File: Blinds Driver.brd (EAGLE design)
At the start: 100 x 80 mm, 29 parts

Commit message: Shrinkage!
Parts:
- moved TIME_DIP 34.2 mm to (14.0, 26.7), turned to 90 degrees
- moved GO_DOWN 20.9 mm to (34.3, 66.0)
- moved GO_UP 18.5 mm to (25.4, 66.0)
- moved R8 12.5 mm to (57.1, 53.3), turned to 270 degrees
- moved ADDLARGETIME 11.7 mm to (52.1, 66.0)
- moved ADDSMALLTIME 11.4 mm to (43.2, 66.0)
- moved D1 6.35 mm to (69.8, 16.5)
- moved D2 6.35 mm to (69.8, 50.8)
- moved D5 6.35 mm to (73.7, 50.8)
- moved D7 6.35 mm to (73.7, 43.2)
- moved D8 6.35 mm to (73.7, 25.4)
- moved MOTOR_OUT 6.35 mm to (87.6, 71.1)
- moved R7 6.35 mm to (59.7, 19.1)
- moved H_BRIDGE 6.35 mm to (61.0, 33.0)
- moved D3 6.35 mm to (76.2, 29.2)
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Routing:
- net N$19: track 30.2 -> 58.2 mm
- net N$18: track 21.2 -> 48.3 mm
- net N$21: track 55.4 -> 32.4 mm
- net N$4: track 19.1 -> 41.3 mm
- net N$5: track 15.5 -> 35.2 mm
- net N$7: track 12.0 -> 27.3 mm
- net +5V: track 112.6 -> 102.4 mm
- net N$20: track 49.8 -> 39.8 mm
- net N$3: track 38.4 -> 30.6 mm
- net N$1: track 29.0 -> 21.2 mm
- net N$22: track 40.9 -> 34.4 mm
- net N$2: track 22.9 -> 16.5 mm
- net N$24: track 46.8 -> 44.5 mm
- net N$9: track 16.3 -> 17.9 mm

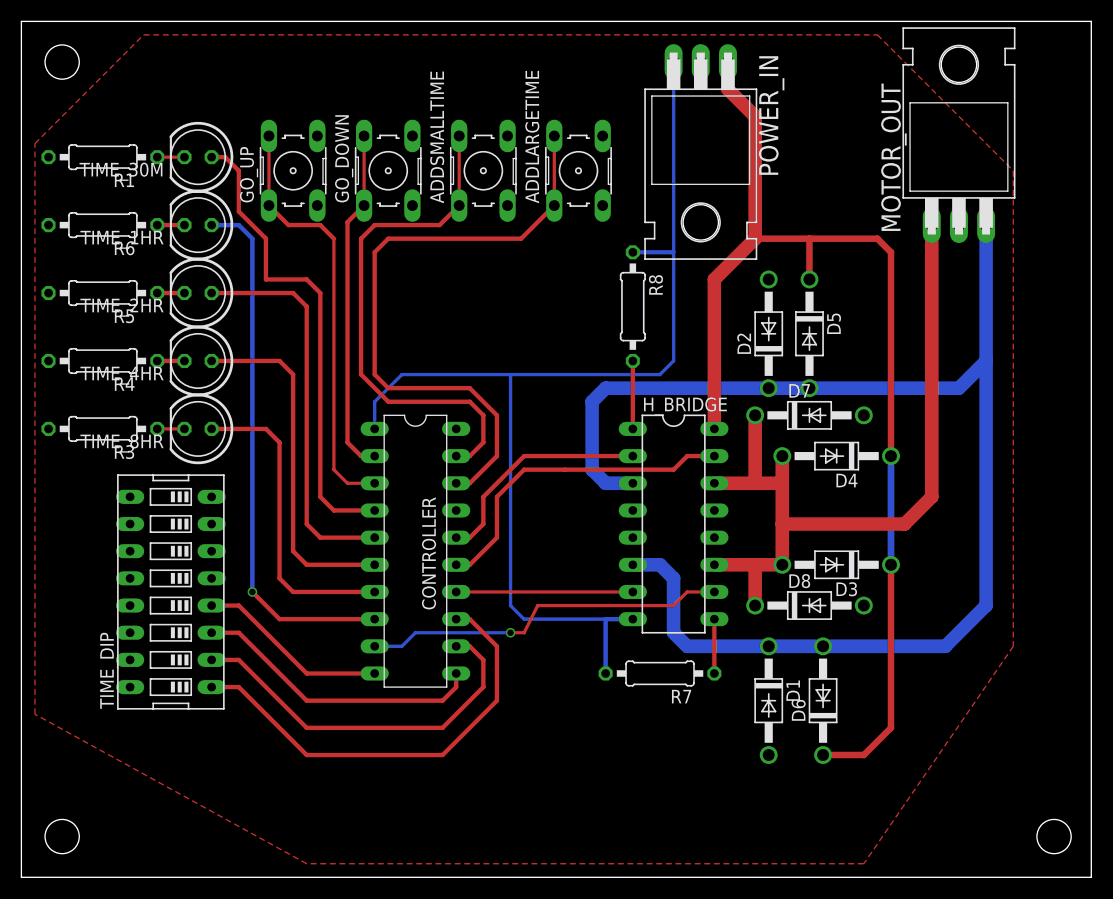
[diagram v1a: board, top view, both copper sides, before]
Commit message: Miniaturize and remove last via
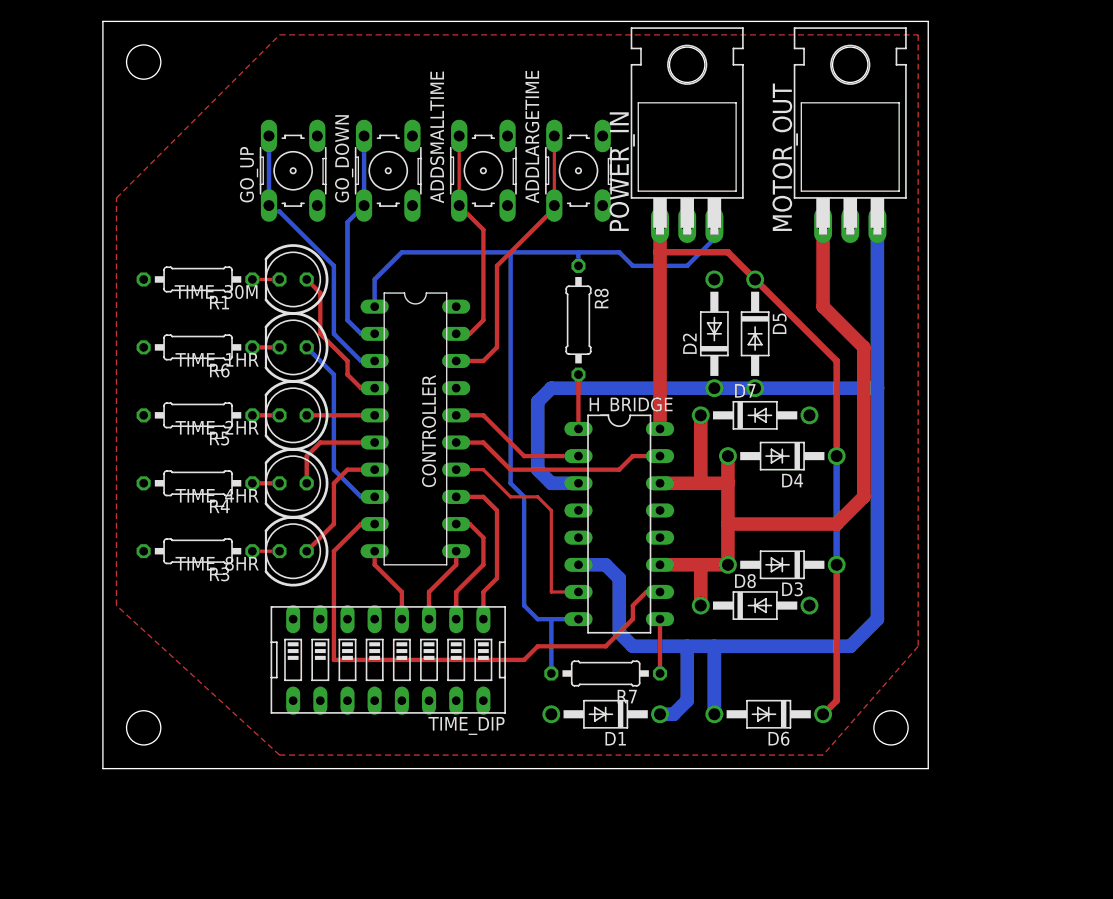
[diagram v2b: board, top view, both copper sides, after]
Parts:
- moved TIME_DIP 21.3 mm to (34.3, 20.3), turned to 180 degrees
- moved D1 15.3 mm to (54.6, 15.2), turned to 180 degrees
- moved R1 14.5 mm to (16.5, 55.9)
- moved R4 14.5 mm to (16.5, 36.8)
- moved R5 14.5 mm to (16.5, 43.2)
- moved R6 14.5 mm to (16.5, 49.5)
- moved R3 14.5 mm to (16.5, 30.5)
- moved TIME_1HR 14.5 mm to (25.4, 49.5)
- moved TIME_2HR 14.5 mm to (25.4, 43.2)
- moved TIME_30M 14.5 mm to (25.4, 55.9)
- moved TIME_4HR 14.5 mm to (25.4, 36.8)
- moved TIME_8HR 14.5 mm to (25.4, 30.5)
- moved CONTROLLER 11.4 mm to (36.8, 41.9)
- moved MOTOR_OUT 10.2 mm to (77.5, 71.1)
- moved D6 5.24 mm to (69.8, 15.2), turned to 180 degrees
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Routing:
- net N$13: track 49.8 -> 17.3 mm, vias 1 -> 0
- net +12V: track 105.8 -> 73.3 mm
- net N$19: track 58.2 -> 26.3 mm
- net N$24: track 44.5 -> 13.5 mm
- net N$12: track 36.6 -> 6.35 mm
- net N$18: track 48.3 -> 21.2 mm
- net N$4: track 41.3 -> 15.0 mm
- net N$5: track 35.2 -> 11.7 mm
- net N$11: track 32.8 -> 9.42 mm
- net N$7: track 27.3 -> 7.40 mm
- net +5V: track 102.4 -> 83.7 mm
- net N$10: track 29.0 -> 11.7 mm
- net N$22: track 34.4 -> 48.9 mm, vias 1 -> 0
- net N$20: track 39.8 -> 26.1 mm
- net N$21: track 32.4 -> 20.9 mm
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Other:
- board size 100 x 80 mm -> 77.1 x 69.8 mm

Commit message: Slightly smaller, changes holes, improve solderability
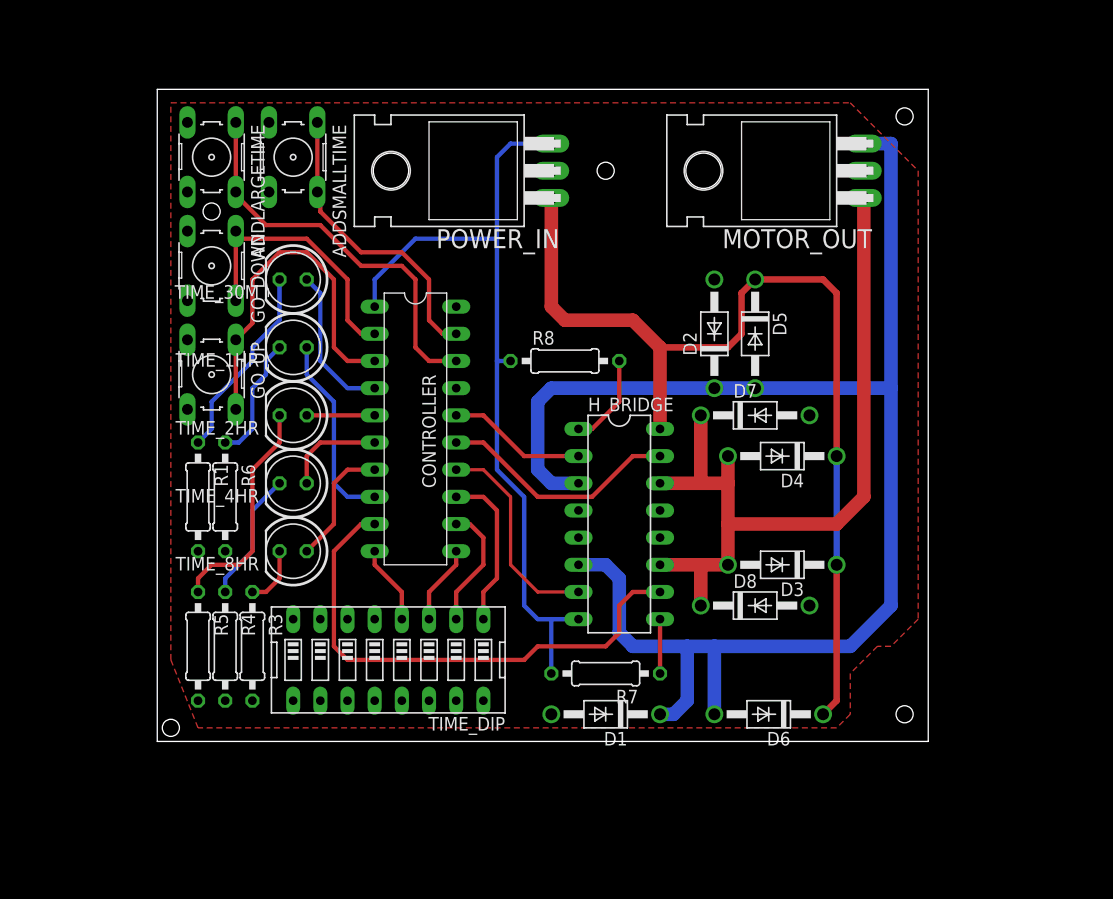
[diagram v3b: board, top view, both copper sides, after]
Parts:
- moved ADDLARGETIME 34.3 mm to (17.8, 67.3), turned to 270 degrees
- moved POWER_IN 23.4 mm to (39.4, 66.0), turned to 90 degrees
- moved R5 21.6 mm to (16.5, 21.6), turned to 270 degrees
- moved GO_UP 20.5 mm to (17.8, 47.0), turned to 270 degrees
- moved R1 20.3 mm to (16.5, 35.6), turned to 270 degrees
- moved GO_DOWN 18.8 mm to (17.8, 57.1), turned to 270 degrees
- moved ADDSMALLTIME 17.8 mm to (25.4, 67.3), turned to 270 degrees
- moved R4 15.5 mm to (19.1, 21.6), turned to 270 degrees
- moved R6 14.2 mm to (19.1, 35.6), turned to 270 degrees
- moved MOTOR_OUT 10.2 mm to (68.6, 66.0), turned to 90 degrees
- moved R3 10.2 mm to (21.6, 21.6), turned to 270 degrees
- moved R8 4.02 mm to (50.8, 48.3), turned to 0 degrees
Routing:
- net N$16: track 2.54 -> 21.2 mm
- net +12V: track 73.3 -> 91.3 mm
- net N$23: track 2.54 -> 18.4 mm
- net N$25: track 129.4 -> 141.4 mm
- net N$19: track 26.3 -> 37.5 mm
- net N$15: track 2.54 -> 12.3 mm
- net N$17: track 2.54 -> 11.7 mm
- net +5V: track 83.7 -> 76.1 mm
- net N$20: track 26.1 -> 33.2 mm
- net N$18: track 21.2 -> 28.1 mm
- net N$21: track 20.9 -> 25.9 mm
- net N$6: track 5.08 -> 8.67 mm
- net N$14: track 2.54 -> 5.61 mm
- net N$3: track 20.6 -> 22.7 mm
- net N$28: track 73.8 -> 74.7 mm
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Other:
- board size 77.1 x 69.8 mm -> 72.1 x 61 mm

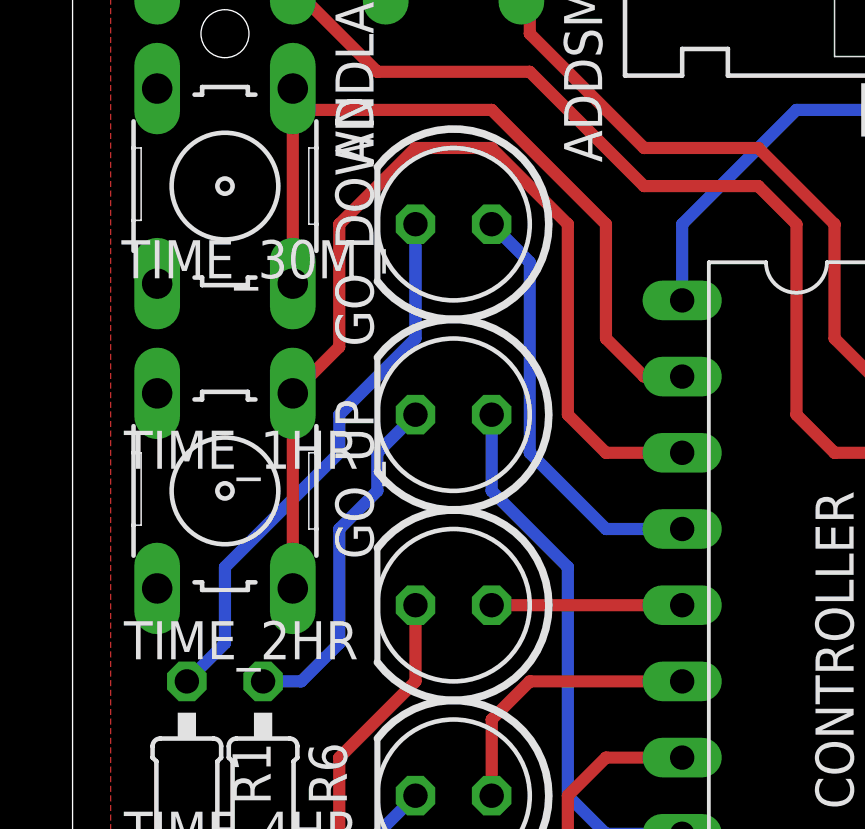
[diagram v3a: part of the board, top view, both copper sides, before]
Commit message: Soldering tweak
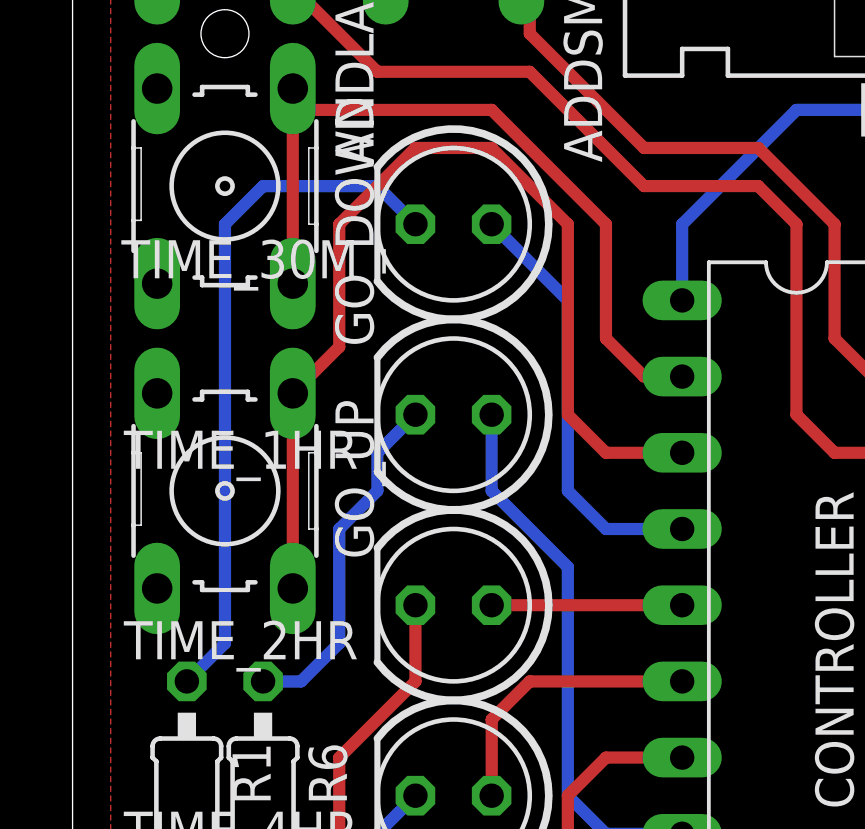
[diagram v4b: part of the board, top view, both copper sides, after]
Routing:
- net N$23: track 18.4 -> 23.2 mm
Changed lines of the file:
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@@
 <contactref element="TIME_30M" pad="K"/>
 <contactref element="R1" pad="1"/>
-<wire x1="24.13" y1="55.88" x2="24.13" y2="52.07" width="0.4064" layer="16"/>
-<wire x1="24.13" y1="52.07" x2="21.59" y2="49.53" width="0.4064" layer="16"/>
-<wire x1="21.59" y1="49.53" x2="21.59" y2="48.26" width="0.4064" layer="16"/>
-<wire x1="21.59" y1="48.26" x2="17.78" y2="44.45" width="0.4064" layer="16"/>
-<wire x1="17.78" y1="44.45" x2="17.78" y2="41.91" width="0.4064" layer="16"/>
+<wire x1="24.13" y1="55.88" x2="22.86" y2="57.15" width="0.4064" layer="16"/>
+<wire x1="22.86" y1="57.15" x2="19.05" y2="57.15" width="0.4064" layer="16"/>
+<wire x1="19.05" y1="57.15" x2="17.78" y2="55.88" width="0.4064" layer="16"/>
+<wire x1="17.78" y1="55.88" x2="17.78" y2="41.91" width="0.4064" layer="16"/>
 <wire x1="17.78" y1="41.91" x2="16.51" y2="40.64" width="0.4064" layer="16"/>
 </signal>
@@
 <contactref element="TIME_30M" pad="A"/>
 <wire x1="33.02" y1="45.72" x2="30.48" y2="45.72" width="0.4064" layer="16"/>
-<wire x1="30.48" y1="45.72" x2="27.94" y2="48.26" width="0.4064" layer="16"/>
-<wire x1="27.94" y1="48.26" x2="27.94" y2="54.61" width="0.4064" layer="16"/>
-<wire x1="27.94" y1="54.61" x2="26.67" y2="55.88" width="0.4064" layer="16"/>
+<wire x1="30.48" y1="45.72" x2="29.21" y2="46.99" width="0.4064" layer="16"/>
+<wire x1="29.21" y1="46.99" x2="29.21" y2="53.34" width="0.4064" layer="16"/>
+<wire x1="29.21" y1="53.34" x2="26.67" y2="55.88" width="0.4064" layer="16"/>
 </signal>
 <signal name="N$4">
